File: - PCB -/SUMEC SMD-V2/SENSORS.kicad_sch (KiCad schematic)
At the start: 20 parts, among them U4 QRE1113, U5 QRE1113, U6 QRE1113

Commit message: cleanup
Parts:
- U4, U5, U6: footprint sumec_library:OnSemi_CASE100AQ - QRE1113 -> (none)
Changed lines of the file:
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@@
       (effects (font (size 1.27 1.27)) (justify left))
     )
-    (property "Footprint" "sumec_library:OnSemi_CASE100AQ - QRE1113" (at 218.44 92.71 0)
+    (property "Footprint" "" (at 218.44 92.71 0)
       (effects (font (size 1.27 1.27)) hide)
     )
@@
       (effects (font (size 1.27 1.27)) (justify left))
     )
-    (property "Footprint" "sumec_library:OnSemi_CASE100AQ - QRE1113" (at 182.88 92.71 0)
+    (property "Footprint" "" (at 182.88 92.71 0)
       (effects (font (size 1.27 1.27)) hide)
     )
@@
       (effects (font (size 1.27 1.27)) (justify left))
     )
-    (property "Footprint" "sumec_library:OnSemi_CASE100AQ - QRE1113" (at 200.66 92.71 0)
-      (effects (font (size 1.27 1.27)) hide)
-    )
+    (property "Footprint" "" (at 200.66 92.71 0)
+      (effects (font (size 1.27 1.27)) hide)
+    )

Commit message: sumec SMD V2 schematic update
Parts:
- removed J?: Conn_01x06_Pin, Connector_JST:JST_SH_BM06B-SRSS-TB_1x06-1MP_P1.00mm_Vertical, symbol Connector:Conn_01x06_Pin
- removed JP1: SolderJumper_3_Open, Jumper:SolderJumper-3_P2.0mm_Open_TrianglePad1.0x1.5mm, symbol Jumper:SolderJumper_3_Open
- removed R? (x3): 100, Resistor_SMD:R_1206_3216Metric, symbol Device:R
- removed R? (x6): 0R, Resistor_SMD:R_1206_3216Metric, symbol Device:R
- removed R? (x3): 10k, Resistor_SMD:R_1206_3216Metric, symbol Device:R
- removed U4, U5, U6: QRE1113, symbol Sensor_Proximity:QRE1113
- removed U?: TSOP382xx, Connector_PinSocket_2.54mm:PinSocket_1x03_P2.54mm_Vertical, symbol Interface_Optical:TSOP382xx
- added J10, J11: Conn_01x03_Pin, Connector_PinHeader_2.54mm:PinHeader_1x03_P2.54mm_Vertical, symbol Connector:Conn_01x03_Pin
- added J3, J4: Conn_01x04_Pin, Connector_Molex:Molex_PicoBlade_53398-0471_1x04-1MP_P1.25mm_Vertical, symbol Connector:Conn_01x04_Pin
- added J?: Conn_01x06_Pin, symbol Connector:Conn_01x06_Pin
- added U4: MPU-9250, Sensor_Motion:InvenSense_QFN-24_3x3mm_P0.4mm, symbol Sensor_Motion:MPU-9250
- added U?: TSOP382xx, Connector_PinSocket_2.54mm:PinSocket_1x03_P2.54mm_Vertical, symbol Interface_Optical:TSOP382xx
- J? (x2): footprint Connector_JST:JST_SH_BM06B-SRSS-TB_1x06-1MP_P1.00mm_Vertical -> (none)
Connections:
- net SENSOR_SUPPLY is gone; now on net +5V: J?.1 (Pin_1), J?.1 (Pin_1)
- net +3V3: now also J10.2 (Pin_2), J11.2 (Pin_2), J3.2 (Pin_2), J4.2 (Pin_2), U?.3 (Vs)
- net +5V: now also J?.1 (Pin_1)
- net GND: now also J?.5 (Pin_5), J?.5 (Pin_5), J10.3 (Pin_3), J11.3 (Pin_3), J3.3 (Pin_3), J4.3 (Pin_3), J?.4 (Pin_4), J?.5 (Pin_5), U?.2 (GND)
- net IR MODULE: now also U?.1 (OUT)
- net QRE1113 B: now also J3.4 (Pin_4)
- net QRE1113 C: now also J4.1 (Pin_1)
- net SCL: now also J?.3 (Pin_3)
- net SDA: now also J?.2 (Pin_2)
- new net QRE1113 A: J3.1 (Pin_1)
- new net SHARP 1: J10.1 (Pin_1)
- new net SHARP 2: J11.1 (Pin_1)
- no-connect marks 3 -> 7
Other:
- note added: "DISTANCE SENSORS"
- note added: "DISTANCE SENSORS - SIDE"
- note added: "IR MODULE"
- note added: "SENZORY ČÁRY"
- note added: "Sharp GP2Y0D810Z0F Digital Distance"
- note added: "conn molex 4pin picoblade pro zadni QRE, 2 conn 1. pro predni board, a 2. pro samostatni qre."
- note added: "gyros scope zapojeni plus text"
- note added: "molex picoblade 6pin"
- note added: "nahore pripajenou rovnou"
- note added: "pojemnovani silkscreen"
- note added: "side-sensors"
- note added: "text, manual atd"
- note added: "zmena: xshut na gnd, supply 5v"
- note removed: "INFRAČERVENÍ MODUL"
- note removed: "SENZORY VZDALENOSTI"
- note removed: "SENZORY ČÁRÝ"
- moved on the sheet: J?

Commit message: pcb schematic update
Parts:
- U?: footprint Connector_PinSocket_2.54mm:PinSocket_1x03_P2.54mm_Vertical -> Connector_Wire:SolderWire-0.1sqmm_1x03_P3.6mm_D0.4mm_OD1mm
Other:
- note removed: "molex picoblade 6pin"
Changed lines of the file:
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@@
   (no_connect (at 90.17 128.27))
   (no_connect (at 209.55 69.85))
-  (no_connect (at 132.08 66.04))
+  (no_connect (at 260.35 26.67))
   (no_connect (at 41.91 128.27))
   (no_connect (at 99.06 27.94))
@@
     (effects (font (size 3 3) bold (color 0 0 0 1)) (justify left bottom))
   )
-  (text "molex picoblade 6pin" (at 72.39 118.11 0)
-    (effects (font (size 1.27 1.27)) (justify left bottom))
-  )
   (text "SENZORY ČÁRY" (at 168.91 21.59 0)
     (effects (font (size 3 3) bold (color 0 0 0 1)) (justify left bottom))
@@
   )
   (text "TF-LUNA MANUAL" (at 25.4 110.49 0)
-    (effects (font (face "Arial Unicode MS") (size 2 2) (thickness 0.254) bold (color 0 0 0 1)) (justify left bottom) (href "https://www.waveshare.com/wiki/TF-Luna_LiDAR_Range_Sensor"))
+    (effects (font (size 2 2) (thickness 0.254) bold) (justify left bottom) (href "https://www.waveshare.com/wiki/TF-Luna_LiDAR_Range_Sensor"))
   )
   (text "DISTANCE SENSORS" (at 41.91 85.09 0)
@@
       (effects (font (size 1.27 1.27)) (justify right))
     )
-    (property "Footprint" "Connector_PinSocket_2.54mm:PinSocket_1x03_P2.54mm_Vertical" (at 52.07 69.215 0)
+    (property "Footprint" "Connector_Wire:SolderWire-0.1sqmm_1x03_P3.6mm_D0.4mm_OD1mm" (at 52.07 69.215 0)
       (effects (font (size 1.27 1.27)) hide)
     )

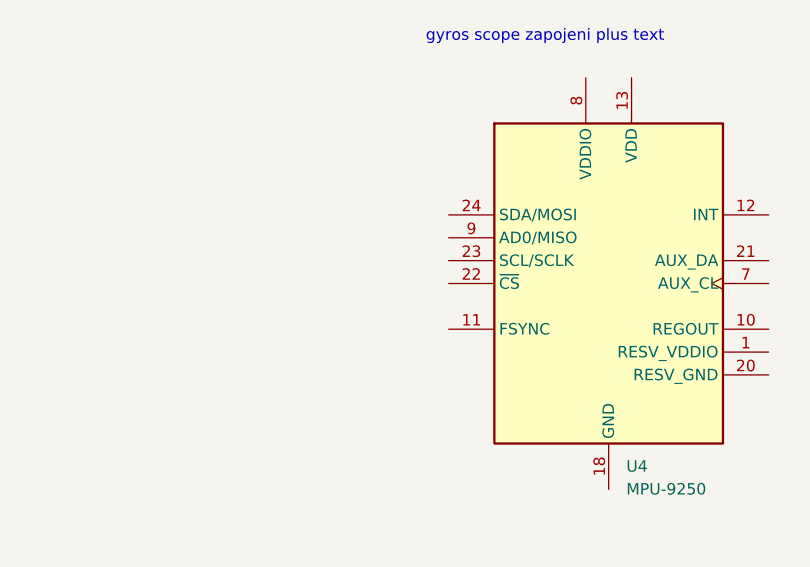
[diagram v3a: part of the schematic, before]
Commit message: SMDV2 - footprints
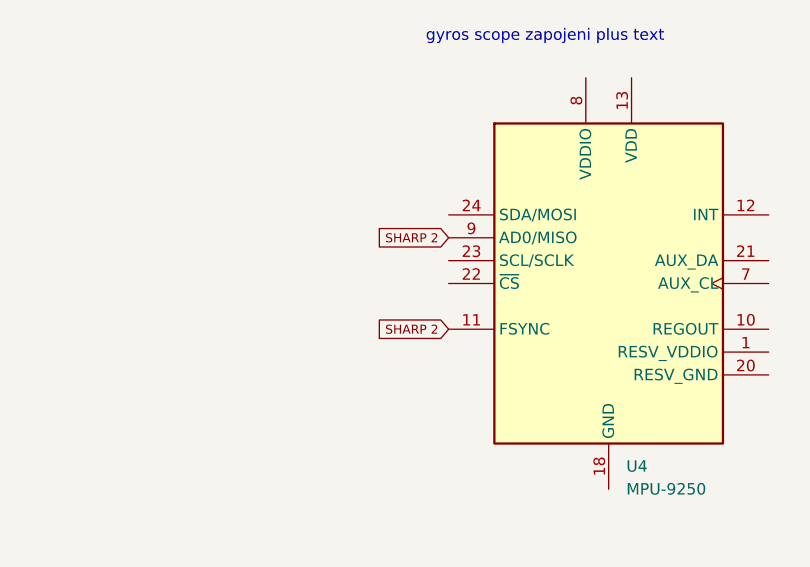
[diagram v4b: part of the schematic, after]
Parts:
- J? (x3): footprint (none) -> Connector_Molex:Molex_PicoBlade_53398-0671_1x06-1MP_P1.25mm_Vertical
- U?: footprint Connector_Wire:SolderWire-0.1sqmm_1x03_P3.6mm_D0.4mm_OD1mm -> Connector_PinSocket_2.54mm:PinSocket_1x03_P2.54mm_Vertical
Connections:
- net SHARP 2: now also U4.11 (FSYNC), U4.9 (AD0/MISO)
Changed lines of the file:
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@@
+    )
+  )
+  (global_label "SHARP 2" (shape input) (at 226.06 113.03 180) (fields_autoplaced)
+    (effects (font (size 1 1) (color 0 0 0 1)) (justify right))
+    (property "Intersheetrefs" "${INTERSHEET_REFS}" (at 217.2007 113.03 0)
+      (effects (font (size 1.27 1.27)) (justify right) hide)
     )
   )
@@
     (effects (font (size 1 1) (color 0 0 0 1)) (justify right))
     (property "Intersheetrefs" "${INTERSHEET_REFS}" (at 35.5902 135.89 0)
+      (effects (font (size 1.27 1.27)) (justify right) hide)
+    )
+  )
+  (global_label "SHARP 2" (shape input) (at 226.06 123.19 180) (fields_autoplaced)
+    (effects (font (size 1 1) (color 0 0 0 1)) (justify right))
+    (property "Intersheetrefs" "${INTERSHEET_REFS}" (at 217.2007 123.19 0)
       (effects (font (size 1.27 1.27)) (justify right) hide)
     )
@@
       (effects (font (size 1.27 1.27)) (justify right) hide)
     )
-    (property "Footprint" "" (at 97.79 135.89 0)
+    (property "Footprint" "Connector_Molex:Molex_PicoBlade_53398-0671_1x06-1MP_P1.25mm_Vertical" (at 97.79 135.89 0)
       (effects (font (size 1.27 1.27)) hide)
     )
@@
       (effects (font (size 1.27 1.27)) (justify right) hide)
     )
-    (property "Footprint" "" (at 73.66 135.89 0)
+    (property "Footprint" "Connector_Molex:Molex_PicoBlade_53398-0671_1x06-1MP_P1.25mm_Vertical" (at 73.66 135.89 0)
       (effects (font (size 1.27 1.27)) hide)
     )
@@
       (effects (font (size 1.27 1.27)) (justify right))
     )
-    (property "Footprint" "Connector_Wire:SolderWire-0.1sqmm_1x03_P3.6mm_D0.4mm_OD1mm" (at 52.07 69.215 0)
+    (property "Footprint" "Connector_PinSocket_2.54mm:PinSocket_1x03_P2.54mm_Vertical" (at 52.07 69.215 0)
       (effects (font (size 1.27 1.27)) hide)
     )
@@
       (effects (font (size 1.27 1.27)) (justify right) hide)
     )
-    (property "Footprint" "" (at 49.53 135.89 0)
-      (effects (font (size 1.27 1.27)) hide)
-    )
+    (property "Footprint" "Connector_Molex:Molex_PicoBlade_53398-0671_1x06-1MP_P1.25mm_Vertical" (at 49.53 135.89 0)
+      (effects (font (size 1.27 1.27)) hide)
+    )

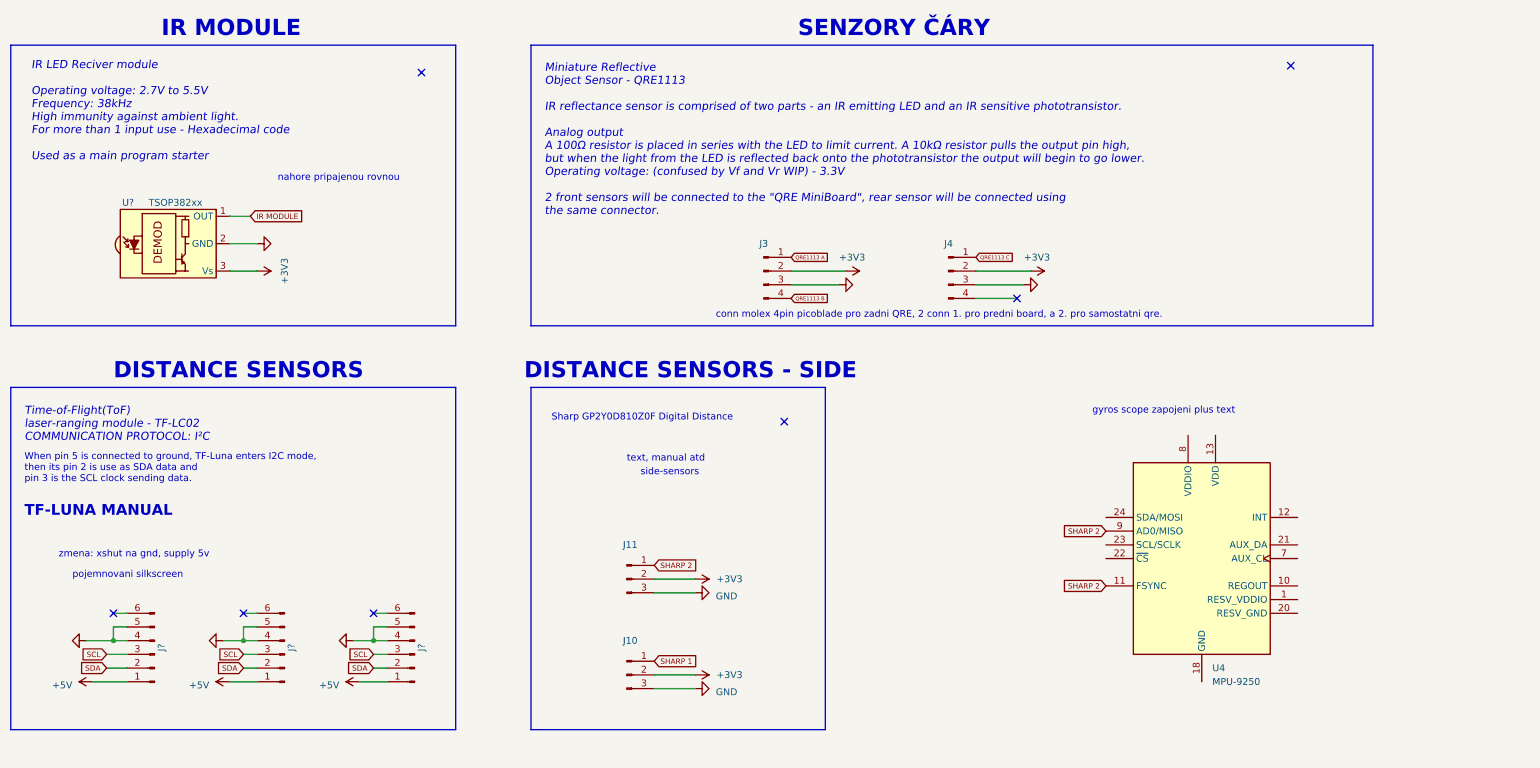
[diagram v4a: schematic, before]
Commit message: Updates:
GyroScope project file, QRE1113 Board update and BOM, SMDv2 iBOM and schematic update.
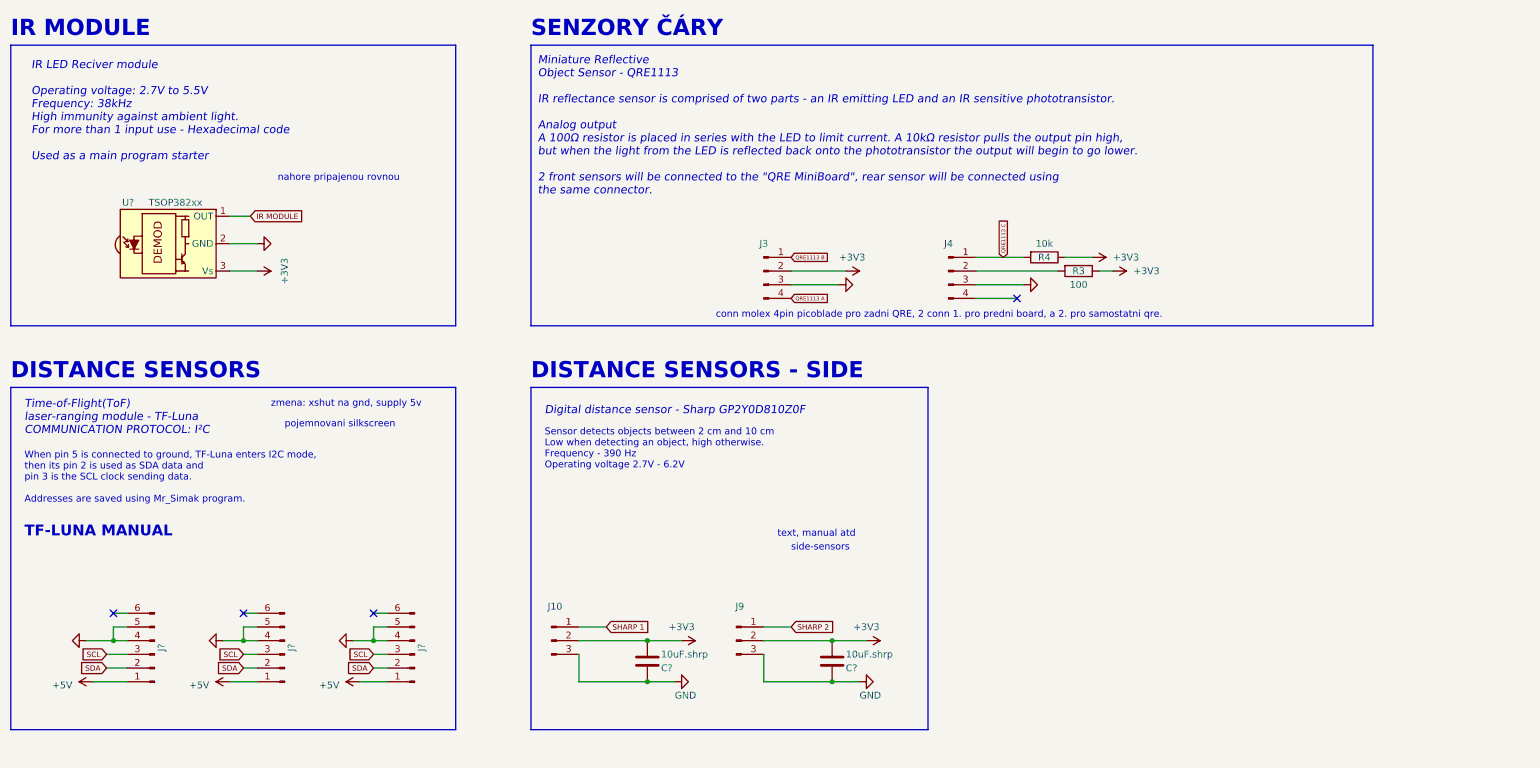
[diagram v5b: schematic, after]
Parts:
- removed J11: Conn_01x03_Pin, Connector_PinHeader_2.54mm:PinHeader_1x03_P2.54mm_Vertical, symbol Connector:Conn_01x03_Pin
- removed U4: MPU-9250, Sensor_Motion:InvenSense_QFN-24_3x3mm_P0.4mm, symbol Sensor_Motion:MPU-9250
- added C? (x2): 10uF.shrp, Capacitor_SMD:C_0805_2012Metric_Pad1.18x1.45mm_HandSolder, symbol Device:C
- added J9: Conn_01x03_Pin, Connector_JST:JST_XH_B3B-XH-A_1x03_P2.50mm_Vertical, symbol Connector:Conn_01x03_Pin
- added R3: 100, Resistor_SMD:R_0805_2012Metric_Pad1.20x1.40mm_HandSolder, symbol Device:R
- added R4: 10k, Resistor_SMD:R_0805_2012Metric_Pad1.20x1.40mm_HandSolder, symbol Device:R
- J10: footprint Connector_PinHeader_2.54mm:PinHeader_1x03_P2.54mm_Vertical -> Connector_JST:JST_XH_B3B-XH-A_1x03_P2.50mm_Vertical
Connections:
- net +3V3: now also C?.2, C?.2, J9.2 (Pin_2), R3.1, R4.1; no longer J4.2 (Pin_2)
- net GND: now also C?.1, C?.1, J9.3 (Pin_3)
- net QRE1113 A: now also J3.4 (Pin_4); no longer J3.1 (Pin_1)
- net QRE1113 B: now also J3.1 (Pin_1); no longer J3.4 (Pin_4)
- net QRE1113 C: now also R4.2
- net SHARP 2: now also J9.1 (Pin_1)
- new net: J4.2 (Pin_2), R3.2
- no-connect marks 7 -> 4
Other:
- note added: "Digital distance sensor - Sharp GP2Y0D810Z0F"
- note added: "Miniature Reflective Object Sensor - QRE1113 IR reflectance sensor is comprised of two parts - an IR emitting LED and an IR sensitive phototransistor. Analog output A 100Ω resistor is placed in series with the LED to limit current. A 10kΩ resistor pulls the output pin high, but when the light from the LED is reflected back onto the phototransistor the output will begin to go lower. 2 front sensor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"
- note added: "Sensor detects objects between 2 cm and 10 cm Low when detecting an object, high otherwise. Frequency - 390 Hz Operating voltage 2.7V - 6.2V"
- note added: "Time-of-Flight(ToF) laser-ranging module - TF-Luna COMMUNICATION PROTOCOL: I²C"
- note added: "When pin 5 is connected to ground, TF-Luna enters I2C mode, then its pin 2 is used as SDA data and pin 3 is the SCL clock sending data. Addresses are saved using Mr_Simak program."
- note removed: "Miniature Reflective Object Sensor - QRE1113 IR reflectance sensor is comprised of two parts - an IR emitting LED and an IR sensitive phototransistor. Analog output A 100Ω resistor is placed in series with the LED to limit current. A 10kΩ resistor pulls the output pin high, but when the light from the LED is reflected back onto the phototransistor the output will begin to go lower. Operating volt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"
- note removed: "Sharp GP2Y0D810Z0F Digital Distance"
- note removed: "Time-of-Flight(ToF) laser-ranging module - TF-LC02 COMMUNICATION PROTOCOL: I²C"
- note removed: "When pin 5 is connected to ground, TF-Luna enters I2C mode, then its pin 2 is use as SDA data and pin 3 is the SCL clock sending data."
- note removed: "gyros scope zapojeni plus text"
- moved on the sheet: J10

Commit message: SMDv2 Schematic update
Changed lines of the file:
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@@
     (stroke (width 0) (type default))
   )
-  (wire (pts (xy 67.31 54.61) (xy 63.5 54.61))
+  (wire (pts (xy 68.58 54.61) (xy 63.5 54.61))
     (stroke (width 0) (type default))
   )
@@
     )
   )
-  (global_label "IR MODULE" (shape input) (at 67.31 54.61 0) (fields_autoplaced)
+  (global_label "IR MODULE" (shape input) (at 68.58 54.61 0) (fields_autoplaced)
     (effects (font (size 1 1) (color 0 0 0 1)) (justify left))
-    (property "Intersheetrefs" "${INTERSHEET_REFS}" (at 77.7884 54.61 0)
+    (property "Intersheetrefs" "${INTERSHEET_REFS}" (at 79.0584 54.61 0)
       (effects (font (size 1.27 1.27)) (justify left) hide)
     )

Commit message: schematic miniupdate
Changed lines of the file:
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@@
       (effects (font (size 1.27 1.27)) hide)
     )
-    (property "Value" "+3V3" (at 176.53 62.23 90)
+    (property "Value" "+3V3" (at 181.61 64.77 90)
       (effects (font (size 1.27 1.27)) (justify left))
     )
